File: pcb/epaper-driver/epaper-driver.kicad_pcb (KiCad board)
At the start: 4 copper layers, 50 x 30.4 mm, 29 parts, among them J1 Conn_01x10, J2 Conn_01x24, J3 Conn_01x05, J4 Conn_01x05, Q1 BSS138, U1 AP2151W

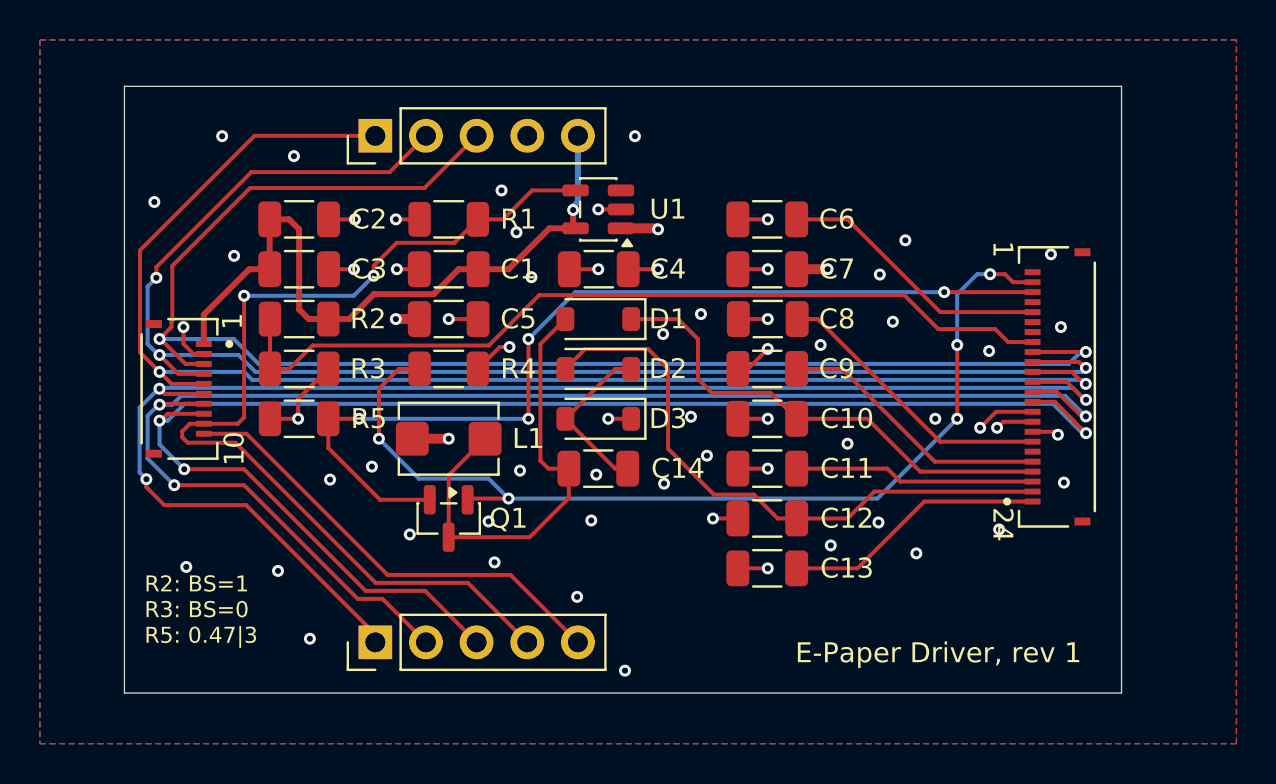
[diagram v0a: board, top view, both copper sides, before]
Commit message: Add pcb for e module
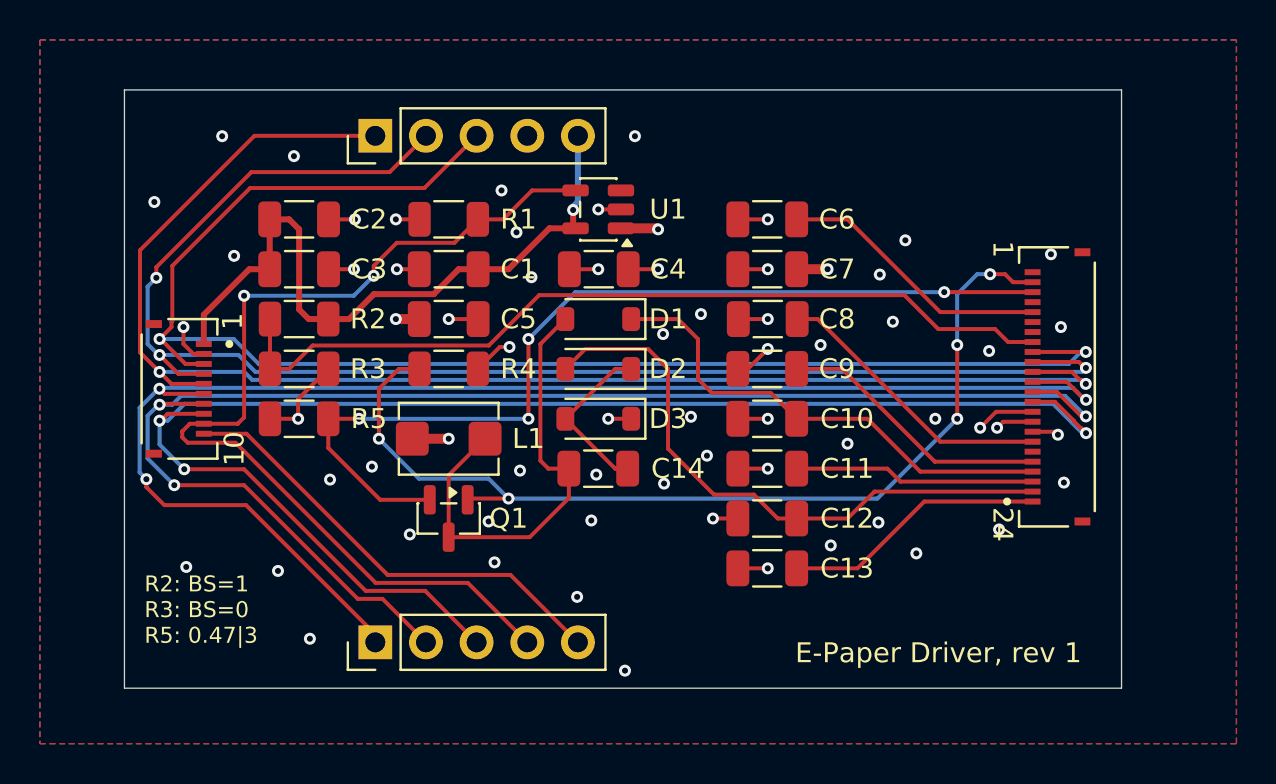
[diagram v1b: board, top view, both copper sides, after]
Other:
- board size 50 x 30.4 mm -> 50 x 30 mm
